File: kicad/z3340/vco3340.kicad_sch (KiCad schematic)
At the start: 63 parts, among them Q1 2N7002, Q2 2N7002, U1 DG442CY+, U2 AS3340, U3 LM79L05, U4 LM311, U5 TL074, U7 LM4040B-5, U8 DG442CY+

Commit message: cleanup references after file renaming
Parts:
- RV1, RV2: symbol as3340:R_POT_TRIM-Device -> z3340:R_POT_TRIM-Device
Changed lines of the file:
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@@
     )
   )
-  (symbol (lib_id "as3340:R_POT_TRIM-Device") (at 294.64 158.75 0) (unit 1)
+  (symbol (lib_id "z3340:R_POT_TRIM-Device") (at 294.64 158.75 0) (unit 1)
     (in_bom yes) (on_board yes) (dnp no)
     (property "Reference" "RV1" (at 291.465 156.845 0)
@@
     )
   )
-  (symbol (lib_id "as3340:R_POT_TRIM-Device") (at 50.8 31.75 0) (unit 1)
+  (symbol (lib_id "z3340:R_POT_TRIM-Device") (at 50.8 31.75 0) (unit 1)
     (in_bom yes) (on_board yes) (dnp no)
     (property "Reference" "RV2" (at 49.022 30.5816 0)

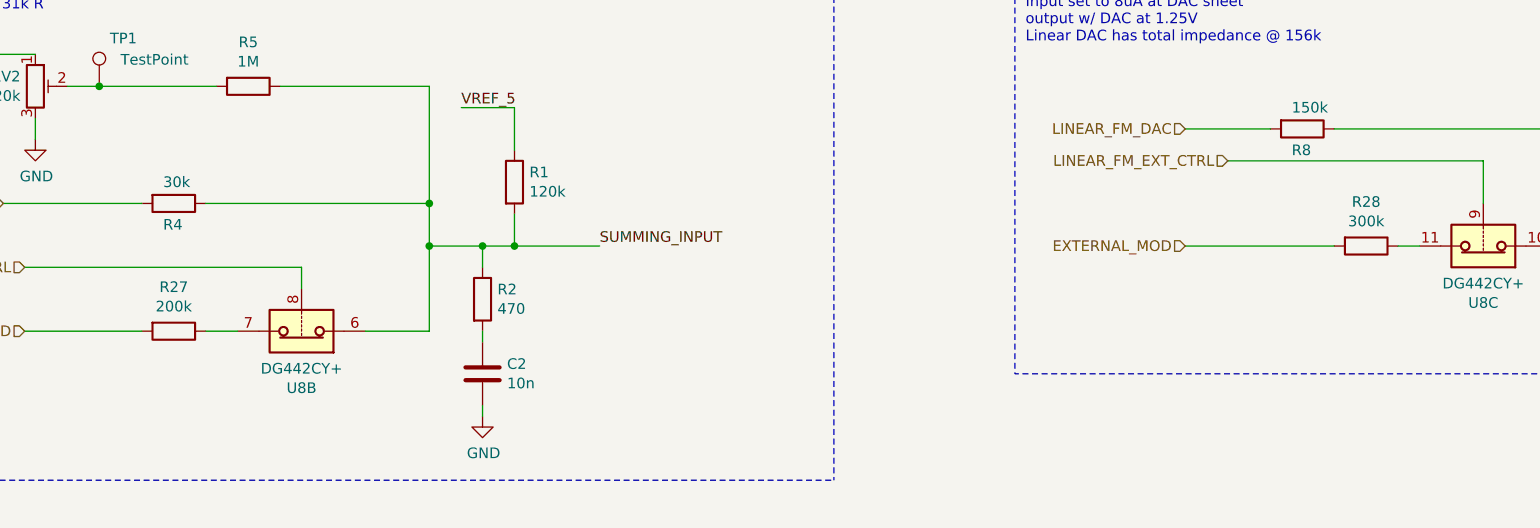
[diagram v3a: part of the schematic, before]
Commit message: checkpoint for z3340 v0.9.  Fixed lm4040 resistor, exp modulation level; removed polygons from routing
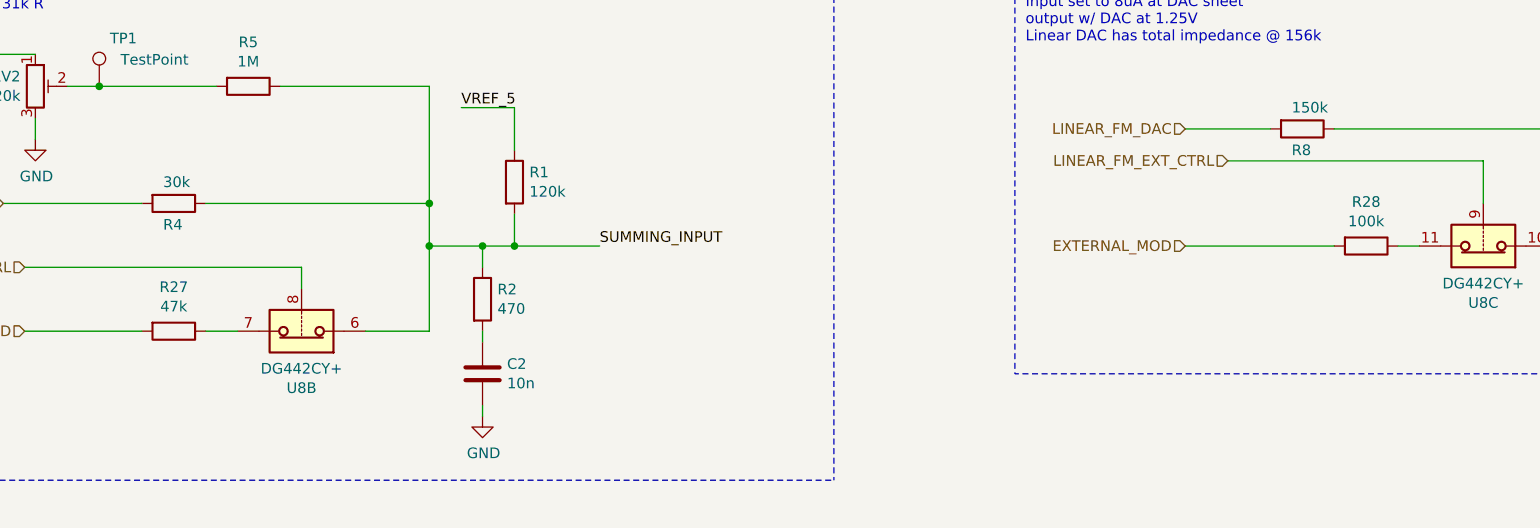
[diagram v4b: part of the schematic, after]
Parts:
- R27: value 200k -> 47k; LCSC Part C25811 -> C25819
- R28: value 300k -> 100k; LCSC Part (none) -> C25803
- R62: LCSC Part (none) -> C25803
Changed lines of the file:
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@@
       (effects (font (size 1.27 1.27)))
     )
-    (property "Value" "200k" (at 67.31 58.0136 90)
+    (property "Value" "47k" (at 67.31 58.0136 90)
       (effects (font (size 1.27 1.27)))
     )
@@
       (effects (font (size 1.27 1.27)) hide)
     )
-    (property "LCSC Part" "C25811" (at 67.31 60.96 0)
+    (property "LCSC Part" "C25819" (at 67.31 60.96 0)
       (effects (font (size 1.27 1.27)) hide)
     )
@@
       (effects (font (size 1.27 1.27)))
     )
-    (property "Value" "300k" (at 209.55 47.8536 90)
+    (property "Value" "100k" (at 209.55 47.8536 90)
       (effects (font (size 1.27 1.27)))
     )
@@
       (effects (font (size 1.27 1.27)) hide)
     )
-    (property "LCSC Part" "" (at 209.55 50.8 0)
+    (property "LCSC Part" "C25803" (at 209.55 50.8 0)
       (effects (font (size 1.27 1.27)) hide)
     )
@@
       (effects (font (size 1.27 1.27)) hide)
     )
-    (property "LCSC Part" "" (at 59.69 163.83 0)
-      (effects (font (size 1.27 1.27)) hide)
-    )
+    (property "LCSC Part" "C25803" (at 59.69 163.83 0)
+      (effects (font (size 1.27 1.27)) hide)
+    )

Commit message: updates for v0.9: polygons, LED resistor, mod amount
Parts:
- C1, C11, C14, C17, C26, C29: LCSC (none) -> C14663; LCSC Part C14663 -> (none)
- C10, C2, C20, C5, C7: LCSC (none) -> C57112; LCSC Part C57112 -> (none)
- C18: LCSC (none) -> C15849; LCSC Part C15849 -> (none)
- C31: LCSC (none) -> C1603; LCSC Part C1603 -> (none)
- C6, C8: LCSC (none) -> C1848; LCSC Part C1848 -> (none)
- D1, D2, D3: LCSC (none) -> C81598; LCSC Part C81598 -> (none)
- Q1, Q2: LCSC (none) -> C8545; LCSC Part C8545 -> (none)
- R1: LCSC (none) -> C25808; LCSC Part C25808 -> (none)
- R11, R15, R31, R32, R7, R9: LCSC (none) -> C25804; LCSC Part C25804 -> (none)
- R12, R13: LCSC (none) -> C23206; LCSC Part C23206 -> (none)
- R19: LCSC (none) -> C4216; LCSC Part C4216 -> (none)
- R2, R6: LCSC (none) -> C23179; LCSC Part C23179 -> (none)
- R20: LCSC (none) -> C23352; LCSC Part C23352 -> (none)
- R21: LCSC (none) -> C23189; LCSC Part C23189 -> (none)
- R25: LCSC (none) -> C23254; LCSC Part C23254 -> (none)
- R26, R34, R5: LCSC (none) -> C22935; LCSC Part C22935 -> (none)
- R27: LCSC (none) -> C25819; LCSC Part C25819 -> (none)
- R28, R62: LCSC (none) -> C25803; LCSC Part C25803 -> (none)
- R3: LCSC (none) -> C4177; LCSC Part C4177 -> (none)
- R37: LCSC (none) -> C17828; LCSC Part C17828 -> (none)
- R38: LCSC (none) -> C22775; LCSC Part C22775 -> (none)
- R4: LCSC (none) -> C22984; LCSC Part C22984 -> (none)
- R8: LCSC (none) -> C22807; LCSC Part C22807 -> (none)
- U1, U8: LCSC (none) -> C2673321; LCSC Part C2673321 -> (none)
- U4: LCSC (none) -> C12597; LCSC Part C12597 -> (none)
- U5: LCSC (none) -> C96507; LCSC Part C96507 -> (none)
- U7: LCSC (none) -> C69315; LCSC Part C69315 -> (none)

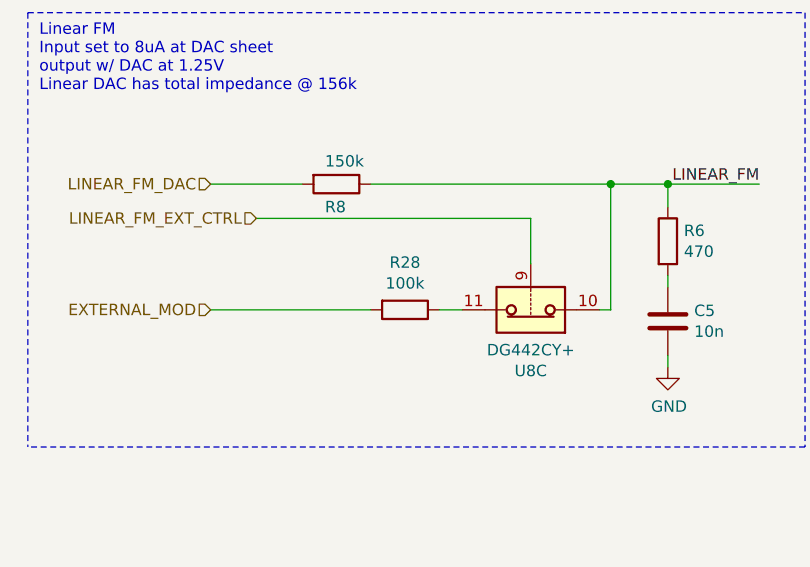
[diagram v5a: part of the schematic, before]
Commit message: changed linear mod amount for z3340, from tame to wild now.  Updated poledancer 2140, better DAC RC filter (higher freq) for 2190.
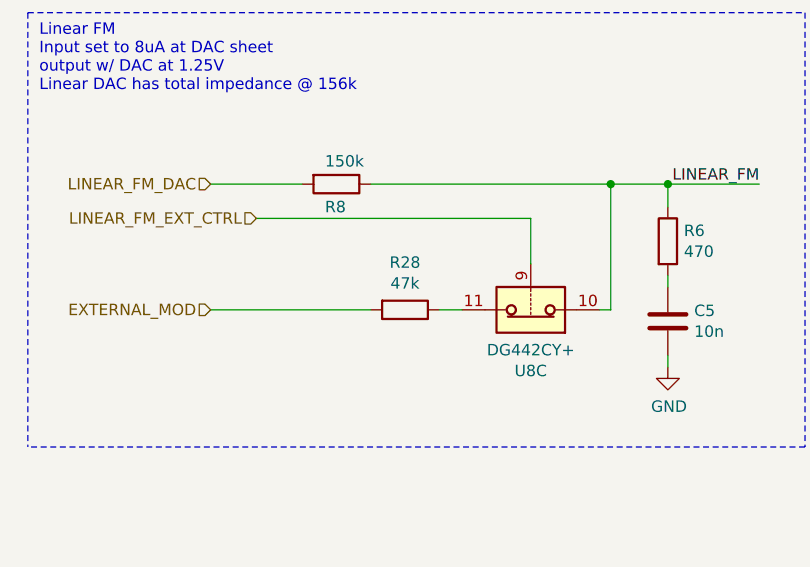
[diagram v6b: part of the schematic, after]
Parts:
- R28: value 100k -> 47k; LCSC C25803 -> C25819
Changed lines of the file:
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@@
       (effects (font (size 1.27 1.27)))
     )
-    (property "Value" "100k" (at 209.55 47.8536 90)
+    (property "Value" "47k" (at 209.55 47.8536 90)
       (effects (font (size 1.27 1.27)))
     )
@@
       (effects (font (size 1.27 1.27)) hide)
     )
-    (property "LCSC" "C25803" (at 209.55 50.8 0)
+    (property "LCSC" "C25819" (at 209.55 50.8 0)
       (effects (font (size 1.27 1.27)) hide)
     )
